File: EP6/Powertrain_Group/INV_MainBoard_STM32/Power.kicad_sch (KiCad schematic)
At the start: 47 parts, among them J14 LVBattery, J3 LVBattery, Q3 AO3400A, U17 AMS1117-3.3, U2 TPS5430DDAR

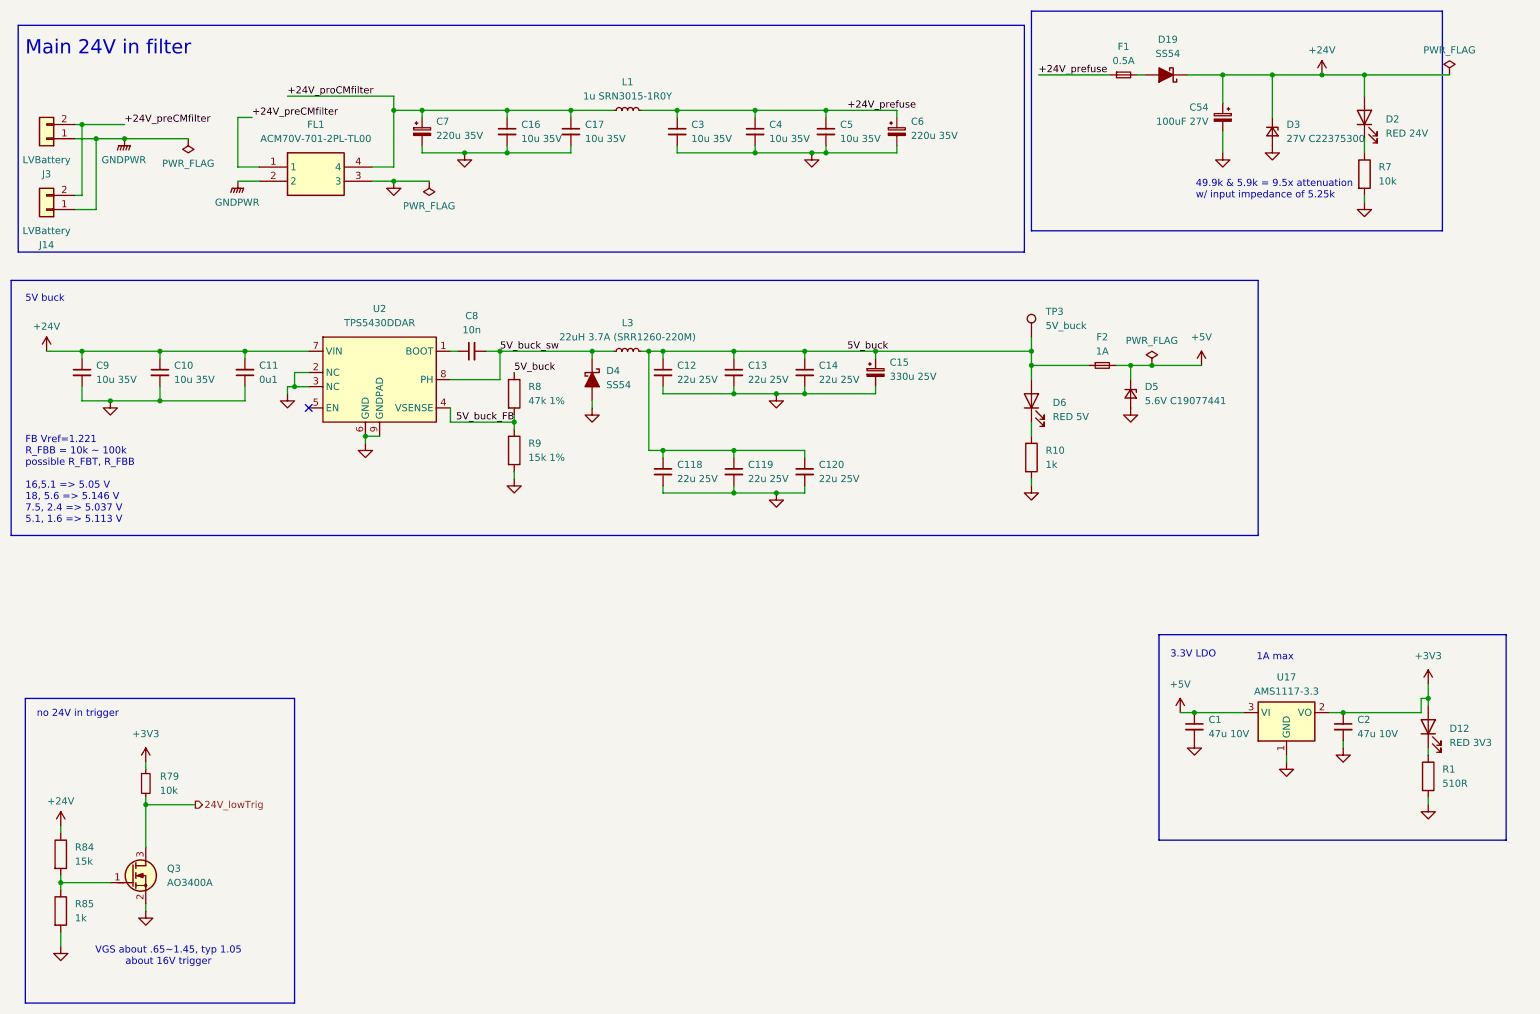
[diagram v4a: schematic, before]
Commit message: update INV_MainBoard_STM32 to V3.0
PCB: INV_MainBoard_STM32 V3.0
V3.0 remove low volte trig
     add RC filt for OCP, OTP
     dedicated OTP, OCP pull down gate enable
     pending: fault hardware OTP/OCP latch
     pending: add QSPI DRAM
     use JST PH
     exterinal pull up for flt, ready
     fix CAN1, 2 label on board
     use 1k, 2k for encoder divider
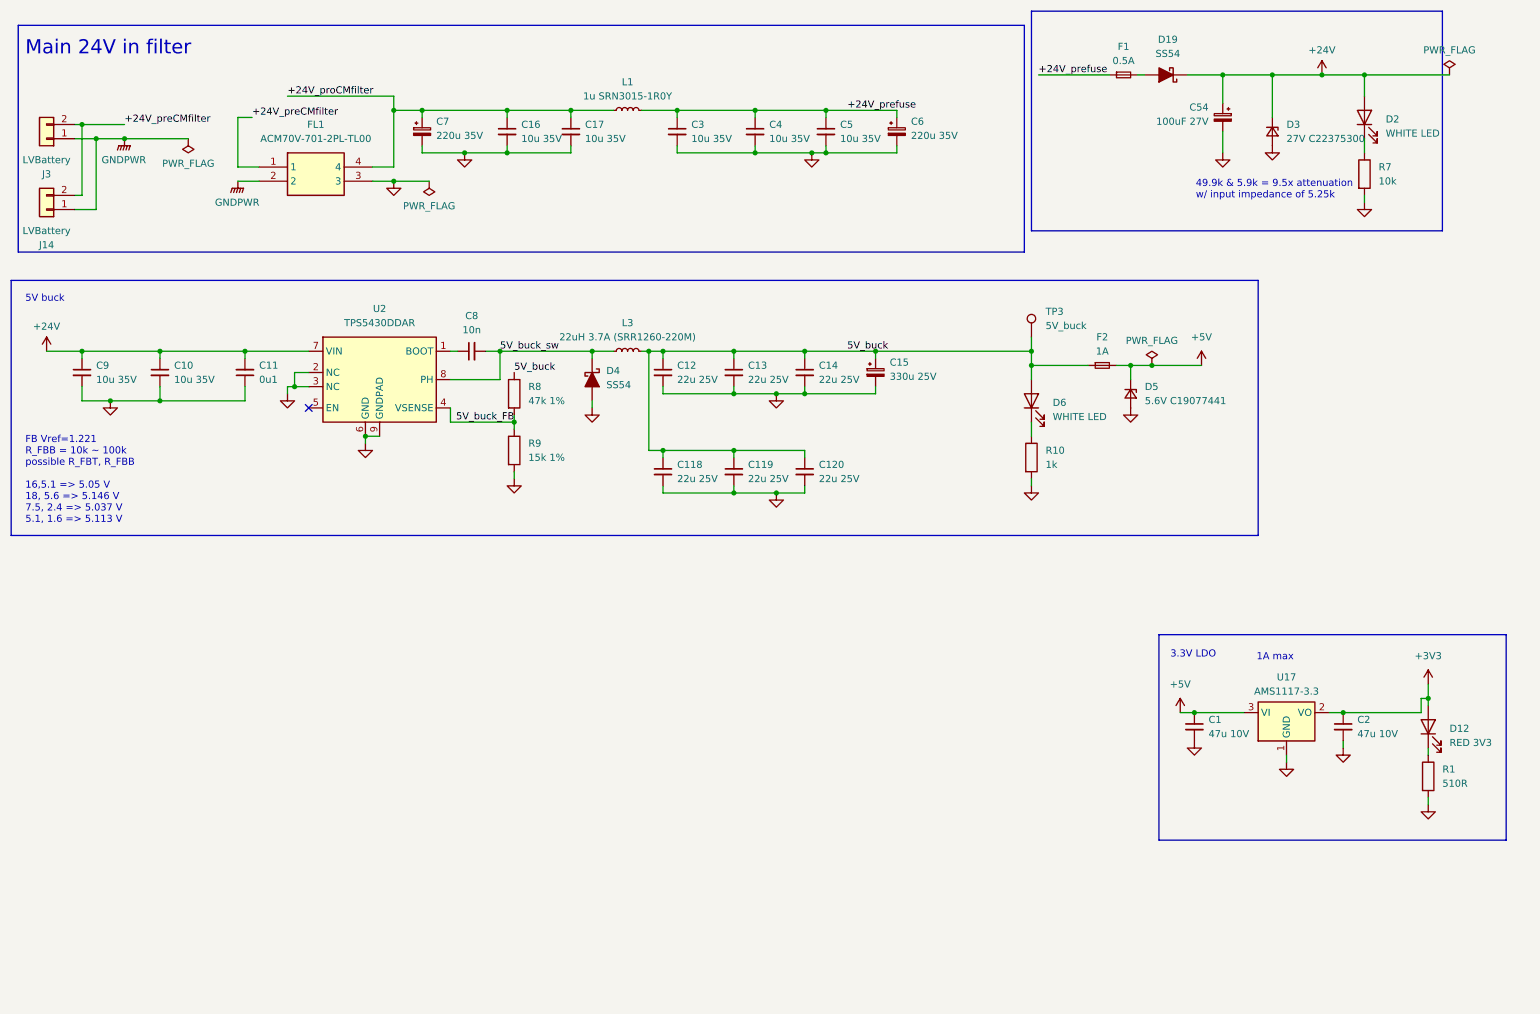
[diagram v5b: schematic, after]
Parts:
- removed Q3: AO3400A, Package_TO_SOT_SMD:SOT-23, symbol PCM_Transistor_MOSFET_AKL:AO3400A
- removed R79: 10k, Resistor_SMD:R_0402_1005Metric, symbol Device:R_Small
- removed R84: 15k, Resistor_SMD:R_0402_1005Metric, symbol Device:R
- removed R85: 1k, Resistor_SMD:R_0402_1005Metric, symbol Device:R
- D2: value RED 24V -> WHITE LED
- D6: value RED 5V -> WHITE LED
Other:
- note removed: "VGS about .65~1.45, typ 1.05 about 16V trigger"
- note removed: "no 24V in trigger"

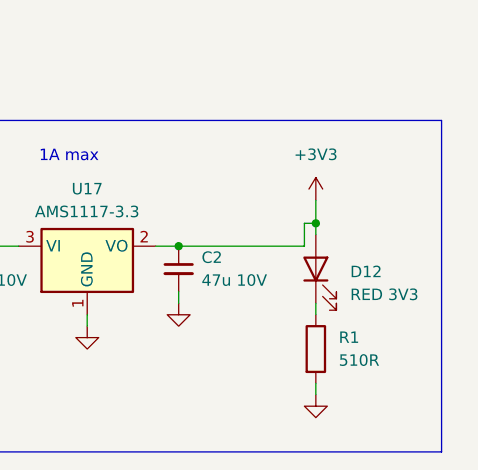
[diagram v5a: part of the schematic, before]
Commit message: update INV_MainBoard_STM32 to V3.1
V3.1 fix R93 to 100R
     add led for OCP, OTP flt
     add default Res for OTP threshold
     add gnd pins for testing
     fix latch circuit
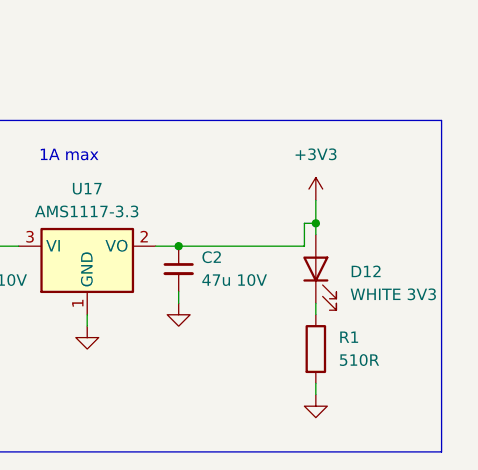
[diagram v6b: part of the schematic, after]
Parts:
- D12: value RED 3V3 -> WHITE 3V3
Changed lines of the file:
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@@
 	(title_block
 		(title "INV_MainBoard_STM32")
-		(date "2025-06-29")
-		(rev "3.0")
+		(date "2025-06-30")
+		(rev "3.1")
 		(company "NTURacing Team")
 		(comment 1 "郭哲明 Jack Kuo")
@@
 		(fields_autoplaced yes)
 		(property "Reference" "D12"
-			(at 271.78 143.8275 90)
+			(at 271.78 143.8274 90)
 			(effects
 				(font
@@
 			)
 		)
-		(property "Value" "RED 3V3"
-			(at 271.78 146.3675 90)
+		(property "Value" "WHITE 3V3"
+			(at 271.78 146.3674 90)
 			(effects
 				(font
